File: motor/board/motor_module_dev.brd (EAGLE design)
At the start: 53.3 x 63.5 mm, 92 parts, among them IC6 LTC6088, IC7 DRV8833RTY

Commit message: Finished layout, round 2
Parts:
- removed I2C_1, I2C_2: (no value), modular_robotics:1X04_2MM_BOARDEDGE
- added JMP_16, JMP_17: (no value), modular_robotics:1X04_NO_SILK
- added R40, R41: 470R, biomimetic:0402-RES
- added R42: 480R, biomimetic:0402-RES
- added U$30: MOTOR_HOUSING, modular_robotics:MOTOR_HOUSING
- PWR_BATT: value JST-RCY-FEMALE -> JST-RCY-FEMALEBATTERY; device modular_robotics:JST_2_FEMALE -> modular_robotics:TP_LIPO_160MAH
- PWR_BUS: value JST-RCY-FEMALE -> JST-RCY-FEMALE-RA
- moved R6 29.9 mm to (37.5, 19.7)
- moved JMP_1 19.7 mm to (47.6, 42.5), turned to 90 degrees
- moved R25 19.1 mm to (38.1, 15.9), turned to 90 degrees
- moved R34 18.2 mm to (34.3, 64.8), flipped to the top, turned to 90 degrees
- moved R39 17.8 mm to (36.8, 15.9), turned to 90 degrees
- moved STATUS_LED 16.6 mm to (37.5, 14.0), turned to 90 degrees
- moved SPI 15.6 mm to (47.6, 38.1)
- moved C6 14.9 mm to (8.26, 34.9), turned to 0 degrees
- moved JMP_0 14.6 mm to (5.71, 43.8), turned to 270 degrees
- moved R11 14.2 mm to (5.71, 31.8), turned to 180 degrees
- moved R2 13.5 mm to (8.26, 33.7), turned to 180 degrees
- moved R10 13.3 mm to (5.71, 30.5), turned to 0 degrees
- moved R27 12.5 mm to (35.6, 64.8), flipped to the top, turned to 90 degrees
- moved R38 12.5 mm to (6.99, 21.0), turned to 0 degrees
- moved R37 12.1 mm to (6.99, 19.7), turned to 0 degrees
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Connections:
- new net N$10: R41.1, SPI.3
- new net N$11: R42.1, SPI.4
- new net N$9: R40.1, SPI.2
- net ARD_A2: now also JMP_16.3, JMP_16.4
- net ARD_A4: now also JMP_17.3, JMP_17.4
- net GND: now also PWR_BATT.V-, U$30.2, U$30.6; no longer I2C_1.2, I2C_2.2, PWR_BATT.1
- net I2C_SCL: now also U$30.3, U$30.7; no longer I2C_1.3, I2C_2.3
- net I2C_SDA: now also U$30.4, U$30.8; no longer I2C_1.4, I2C_2.4
- net MOTOR_A_CURR: now also JMP_16.1, JMP_16.2
- net MOTOR_B_CURR: now also JMP_17.1, JMP_17.2
- net N$1: now also PWR_BATT.V+; no longer PWR_BATT.2
- net SPI_MISO: now also R42.2; no longer SPI.4
- net SPI_MOSI: now also R41.2; no longer SPI.3
- net SPI_SCK: now also R40.2; no longer SPI.2
- net V_3.0: now also U$30.1, U$30.5; no longer I2C_1.1, I2C_2.1
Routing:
- net MOTOR_A_IN1: track 121.2 -> 73.1 mm, vias 6 -> 4
- net MOTOR_B_IN1: track 85.0 -> 56.1 mm, vias 3 -> 2
- net MOTOR_A_CURR: track 22.1 -> 50.5 mm
- net MOTOR_A_IN2: track 96.6 -> 72.0 mm, vias 6 -> 5
- net V_3.0: track 184.6 -> 161.8 mm, vias 8 -> 10
- net SENSE_V_BUS: track 42.6 -> 65.0 mm, vias 0 -> 4
- net ARD_AREF: track 27.2 -> 5.98 mm
- net GND: track 29.4 -> 9.26 mm, vias 7 -> 8
- net MOTOR_B_CURR: track 19.8 -> 38.3 mm, vias 4 -> 6
- net SPI_MISO: track 44.4 -> 29.4 mm, vias 0 -> 1
- net SPI_SS: track 42.0 -> 28.4 mm
- net ARD_5V: track 6.88 -> 19.4 mm
- net SENSE_V_BATT: track 63.3 -> 75.3 mm, vias 1 -> 5
- net N$1: track 11.2 -> 22.8 mm
- net MOTOR_B_BEMF: track 43.1 -> 54.5 mm, vias 3 -> 5
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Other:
- board size 53.3 x 63.5 mm -> 53.3 x 76.2 mm

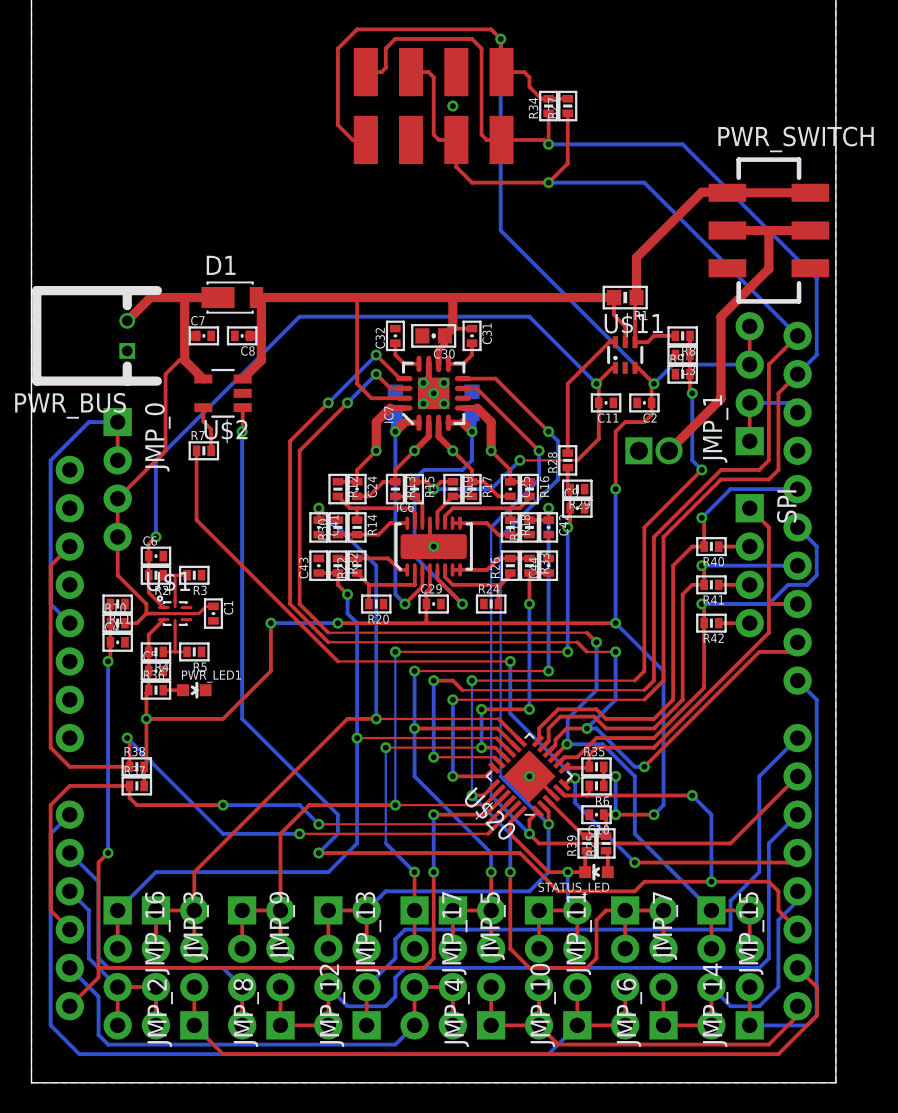
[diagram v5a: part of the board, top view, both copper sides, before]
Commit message: Prepared silkscreen
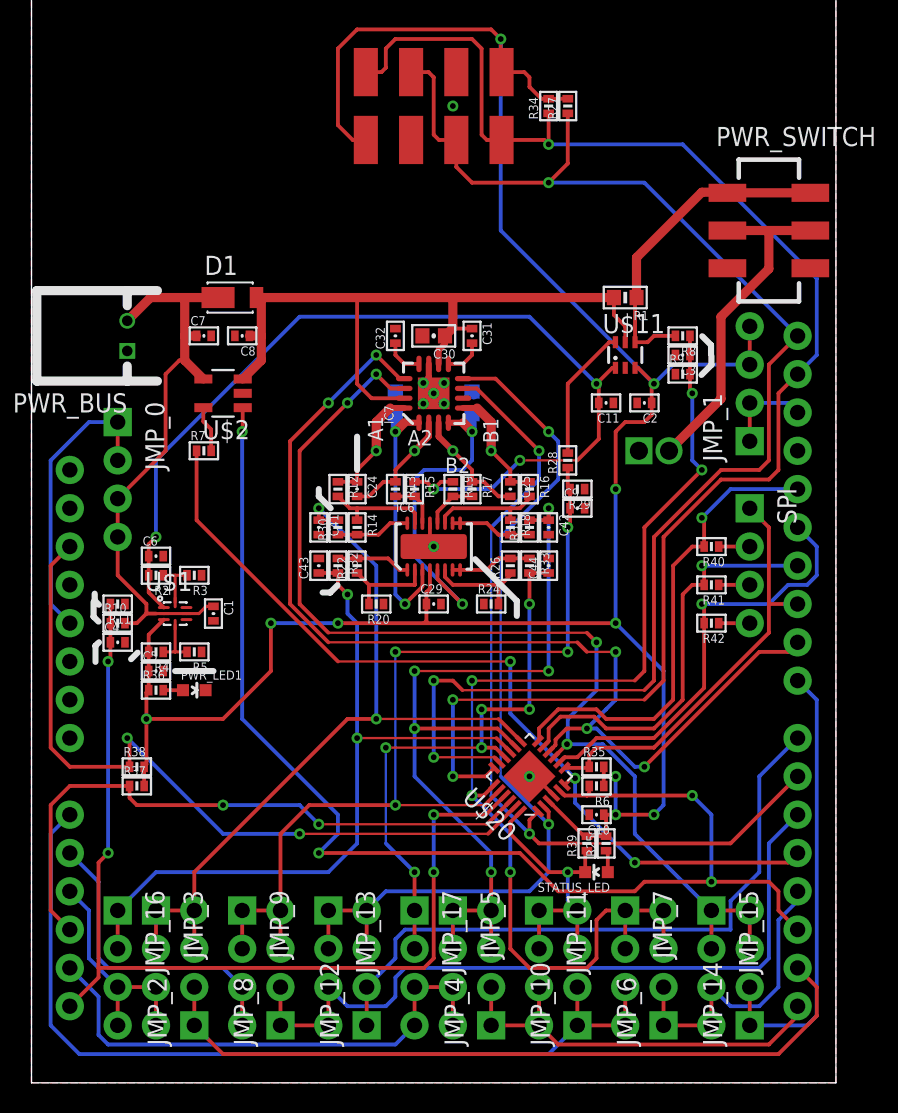
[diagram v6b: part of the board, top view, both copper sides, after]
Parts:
- C24, C25: value 0.1uF -> 100nF
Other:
- board text added: "A1"
- board text added: "A2"
- board text added: "B1"
- board text added: "B2"

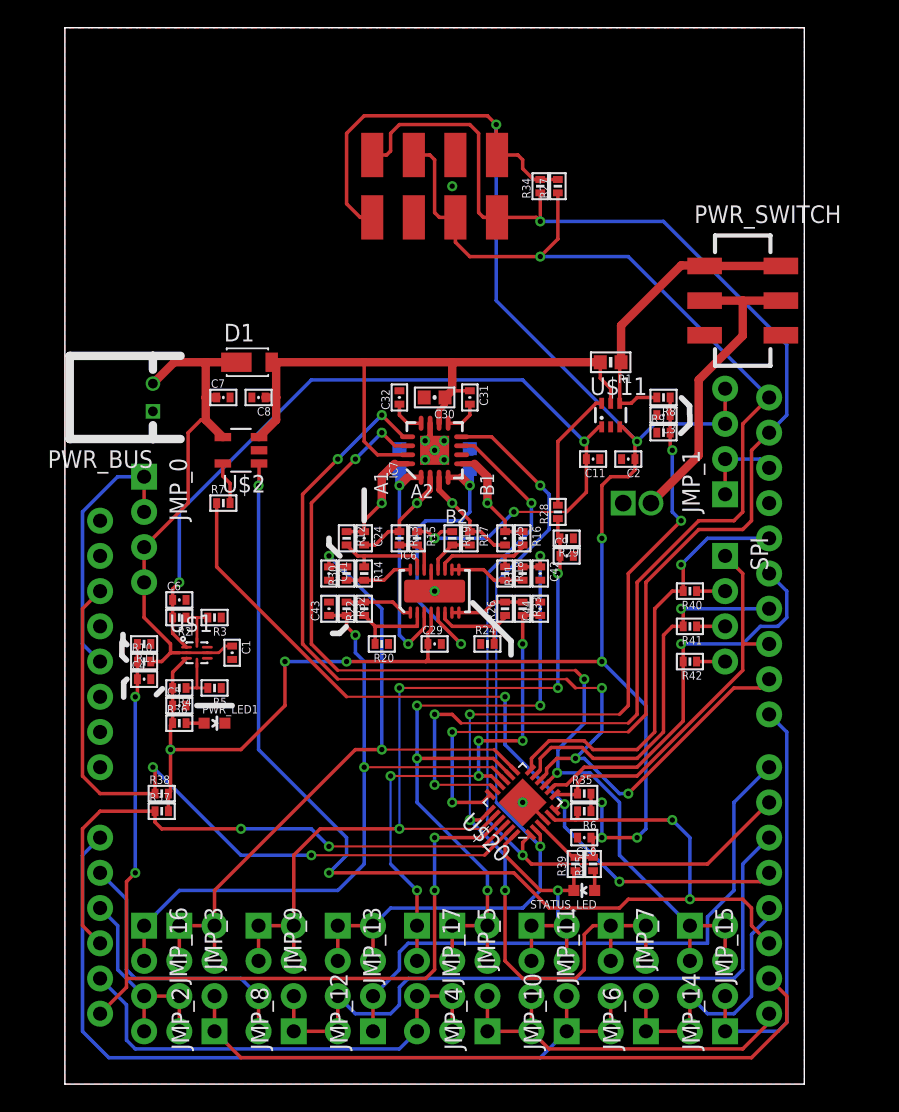
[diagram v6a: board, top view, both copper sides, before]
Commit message: Fixing small things preparing for panelization
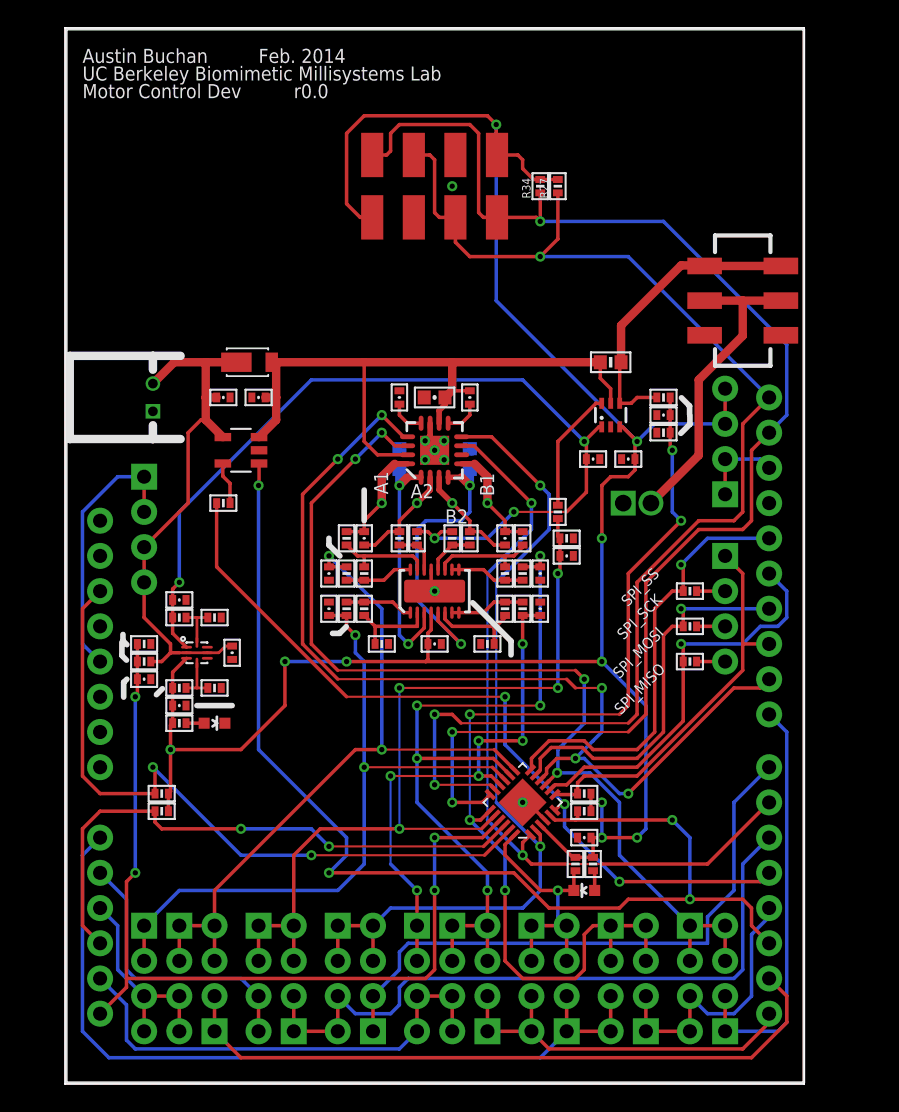
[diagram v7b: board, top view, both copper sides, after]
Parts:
- added U$31: INFO, modular_robotics:INFO
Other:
- board text added: "SPI_MISO"
- board text added: "SPI_MOSI"
- board text added: "SPI_SCK"
- board text added: "SPI_SS"
